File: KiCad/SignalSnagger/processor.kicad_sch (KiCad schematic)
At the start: 78 parts, among them J201 Conn_01x01_Female, J202 Conn_01x01_Female, J203 Conn_01x02, J204 Conn_01x02, J205 Conn_01x01_Female, J206 Conn_01x01_Female, J207 Conn_01x01_Female, J208 Conn_01x01_Female, J209 Conn_01x01_Female, J210 Conn_01x01_Female, J211 Conn_01x01_Female, J212 Conn_01x01_Female, J213 Conn_01x01_Female, J214 Conn_01x01_Female, J215 Conn_01x01_Female, J216 Conn_01x01_Female, J217 Conn_01x01_Female, P201 ISP/PDI, Q201 BSS84W-7-F, Q202 BSS138W-7-F, SW201 SW_SPST, SW202 SW_SPST, SW203 PEC12R-4225F-S0024, U201 AVR128DA48, U202 SI5351, U203 LP2985-5.0, U204 LP2985-3.3, U205 EA_DOGS104W-A, U206 LP2985-5.0, U207 MAX1683EUK, X201 ECS-327TXO-30-TR, X202 25 MHz

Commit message: Ver 0.309
PCB layout updates
Schematic updates
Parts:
- added J218, J219, J220, J221: Conn_01x02, Connector_PinSocket_1.27mm:PinSocket_1x02_P1.27mm_Vertical, symbol Connector_Generic:Conn_01x02
- added SW204, SW205: SW_SPST, Button_Switch_SMD:SW_SPST_TL1014BF160QG, symbol Switch:SW_SPST
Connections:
- net GND: now also J218.1 (Pin_1), J219.1 (Pin_1)
- net PA0: now also J218.2 (Pin_2)
- net PA1: now also J219.2 (Pin_2)
- new net: J221.1 (Pin_1), SW205.1 (A)
- new net: J221.2 (Pin_2), SW205.2 (B)
- new net: J220.1 (Pin_1), SW204.1 (A)
- new net: J220.2 (Pin_2), SW204.2 (B)
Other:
- note removed: "Sense 2"
- moved on the sheet: SW201, SW202

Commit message: Ver 0.310
Schematic and PCB updates
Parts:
- added JP202: Jumper_2_Bridged, Jumper:Jumper_THT-1x02_Bridged_Circular, symbol Jumper:Jumper_2_Bridged_THT
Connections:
- net GND: now also JP202.2 (B); no longer C202.1, C203.1, C205.1, C206.1, C208.2, C209.1, C211.1, C212.1, C213.2, C214.2, C215.2, C216.1, C217.2, C218.1, C219.2, C221.1, D203.1 (K), D204.1 (K), J203.1 (Pin_1), J204.1 (Pin_1), J218.1 (Pin_1), J219.1 (Pin_1), P201.6 (Pin_6), SW201.2 (B), SW202.2 (B), SW203.C, SW203.S2, TP201.1 (Pin_1), U201.15 (GND), U201.29 (GND), U201.43 (GND), U202.8 (GND), U204.2 (GND), U205.12 (IM1), U205.14 (VSS), U205.18 (~{CS}), U205.19 (SA0), X201.2 (GND), X202.2 (GND)
- new net GNDD: C202.1, C203.1, C205.1, C206.1, C208.2, C209.1, C211.1, C212.1, C213.2, C214.2, C215.2, C216.1, C217.2, C218.1, C219.2, C221.1, D203.1 (K), D204.1 (K), J203.1 (Pin_1), J204.1 (Pin_1), J218.1 (Pin_1), J219.1 (Pin_1), JP202.1 (A), P201.6 (Pin_6), SW201.2 (B), SW202.2 (B), SW203.C, SW203.S2, TP201.1 (Pin_1), U201.15 (GND), U201.29 (GND), U201.43 (GND), U202.8 (GND), U204.2 (GND), U205.12 (IM1), U205.14 (VSS), U205.18 (~{CS}), U205.19 (SA0), X201.2 (GND), X202.2 (GND)
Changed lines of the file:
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@@
     (title "SignalSnagger")
     (date "2024-03-18")
-    (rev "0.309")
+    (rev "0.310")
   )
   (bus_alias "PROC_BUS" (members "PA7" "PA6" "PA5" "PA4" "PA3" "PA2" "PA1" "PA0" "PB5" "PB4" "SCL1" "SDA1" "PB1" "PB0" "PC7" "PC6" "PC5" "PC4" "SCL0" "SDA0" "RXD1" "TXD1" "ADC7" "DAC0" "ADC5" "ADC4" "ADC3" "ADC2" "ADC1" "ADC0" "PE3" "PE2" "RXD4" "TXD4" "PF6" "PF5" "PF4" "PF3" "PF2"))
@@
     (stroke (width 0) (type default) (color 0 0 0 0))
   )
+  (wire (pts (xy 36.83 190.5) (xy 36.83 187.96))
+    (stroke (width 0) (type default) (color 0 0 0 0))
+  )
   (wire (pts (xy 240.03 127) (xy 240.03 121.92))
     (stroke (width 0) (type default) (color 0 0 0 0))
@@
     (stroke (width 0) (type default) (color 0 0 0 0))
   )
-  (wire (pts (xy 40.64 190.5) (xy 40.64 189.23))
-    (stroke (width 0) (type default) (color 0 0 0 0))
-  )
   (wire (pts (xy 91.44 55.88) (xy 93.98 55.88))
     (stroke (width 0) (type default) (color 0 0 0 0))
@@
     (stroke (width 0) (type default) (color 0 0 0 0))
   )
-  (wire (pts (xy 45.72 189.23) (xy 45.72 191.77))
-    (stroke (width 0) (type default) (color 0 0 0 0))
-  )
   (wire (pts (xy 266.7 121.92) (xy 274.32 121.92))
     (stroke (width 0) (type default) (color 0 0 0 0))
@@
     (stroke (width 0) (type default) (color 0 0 0 0))
   )
-  (wire (pts (xy 40.64 189.23) (xy 45.72 189.23))
-    (stroke (width 0) (type default) (color 0 0 0 0))
-  )
   (wire (pts (xy 280.67 107.95) (xy 274.32 107.95))
     (stroke (width 0) (type default) (color 0 0 0 0))
@@
     (stroke (width 0) (type default) (color 0 0 0 0))
   )
+  (wire (pts (xy 26.67 190.5) (xy 26.67 187.96))
+    (stroke (width 0) (type default) (color 0 0 0 0))
+  )
   (wire (pts (xy 127 144.78) (xy 132.08 144.78))
     (stroke (width 0) (type default) (color 0 0 0 0))
@@
     (pin "1")
   )
+  (symbol (lib_id "Jumper:Jumper_2_Bridged_THT") (at 31.75 187.96 0) (unit 1)
+    (in_bom yes) (on_board yes)
+    (property "Reference" "JP202" (id 0) (at 31.75 189.23 90)
+      (effects (font (size 1.27 1.27)) (justify right))
+    )
+    (property "Value" "Jumper_2_Bridged" (id 1) (at 31.75 186.1621 0)
+      (effects (font (size 1.27 1.27)) hide)
+    )
+    (property "Footprint" "Jumper:Jumper_THT-1x02_Bridged_Circular" (id 2) (at 31.75 187.96 0)
+      (effects (font (size 1.27 1.27)) hide)
+    )
+    (property "Datasheet" "~" (id 3) (at 31.75 187.96 0)
+      (effects (font (size 1.27 1.27)) hide)
+    )
+    (property "Digi-Key Part No." "N/P" (id 4) (at 31.75 187.96 0)
+      (effects (font (size 1.27 1.27)) hide)
+    )
+    (pin "1")
+    (pin "2")
+  )
   (symbol (lib_id "power:GNDD") (at 147.32 149.86 90) (mirror x) (unit 1)
     (in_bom yes) (on_board yes)
@@
     (pin "1")
   )
-  (symbol (lib_id "power:GNDD") (at 40.64 190.5 0) (unit 1)
+  (symbol (lib_id "power:GNDD") (at 26.67 190.5 0) (unit 1)
     (in_bom yes) (on_board yes) (fields_autoplaced)
-    (property "Reference" "#PWR0259" (id 0) (at 40.64 196.85 0)
+    (property "Reference" "#PWR0259" (id 0) (at 26.67 196.85 0)
       (effects (font (size 1.27 1.27)) hide)
     )
-    (property "Value" "GNDD" (id 1) (at 40.64 194.5624 0))
-    (property "Footprint" "" (id 2) (at 40.64 190.5 0)
+    (property "Value" "GNDD" (id 1) (at 26.67 194.5624 0))
+    (property "Footprint" "" (id 2) (at 26.67 190.5 0)
       (effects (font (size 1.27 1.27)) hide)
     )
-    (property "Datasheet" "" (id 3) (at 40.64 190.5 0)
+    (property "Datasheet" "" (id 3) (at 26.67 190.5 0)
       (effects (font (size 1.27 1.27)) hide)
     )
@@
     (pin "2")
   )
-  (symbol (lib_id "power:GND") (at 45.72 191.77 0) (unit 1)
+  (symbol (lib_id "power:GND") (at 36.83 190.5 0) (unit 1)
     (in_bom yes) (on_board yes) (fields_autoplaced)
-    (property "Reference" "#PWR0260" (id 0) (at 45.72 198.12 0)
-      (effects (font (size 1.27 1.27)) hide)
-    )
-    (property "Value" "GND" (id 1) (at 45.72 196.2134 0)
+    (property "Reference" "#PWR0260" (id 0) (at 36.83 196.85 0)
       (effects (font (size 1.27 1.27)) hide)
     )
-    (property "Footprint" "" (id 2) (at 45.72 191.77 0)
+    (property "Value" "GND" (id 1) (at 36.83 194.9434 0))
+    (property "Footprint" "" (id 2) (at 36.83 190.5 0)
       (effects (font (size 1.27 1.27)) hide)
     )
-    (property "Datasheet" "" (id 3) (at 45.72 191.77 0)
+    (property "Datasheet" "" (id 3) (at 36.83 190.5 0)
       (effects (font (size 1.27 1.27)) hide)
     )

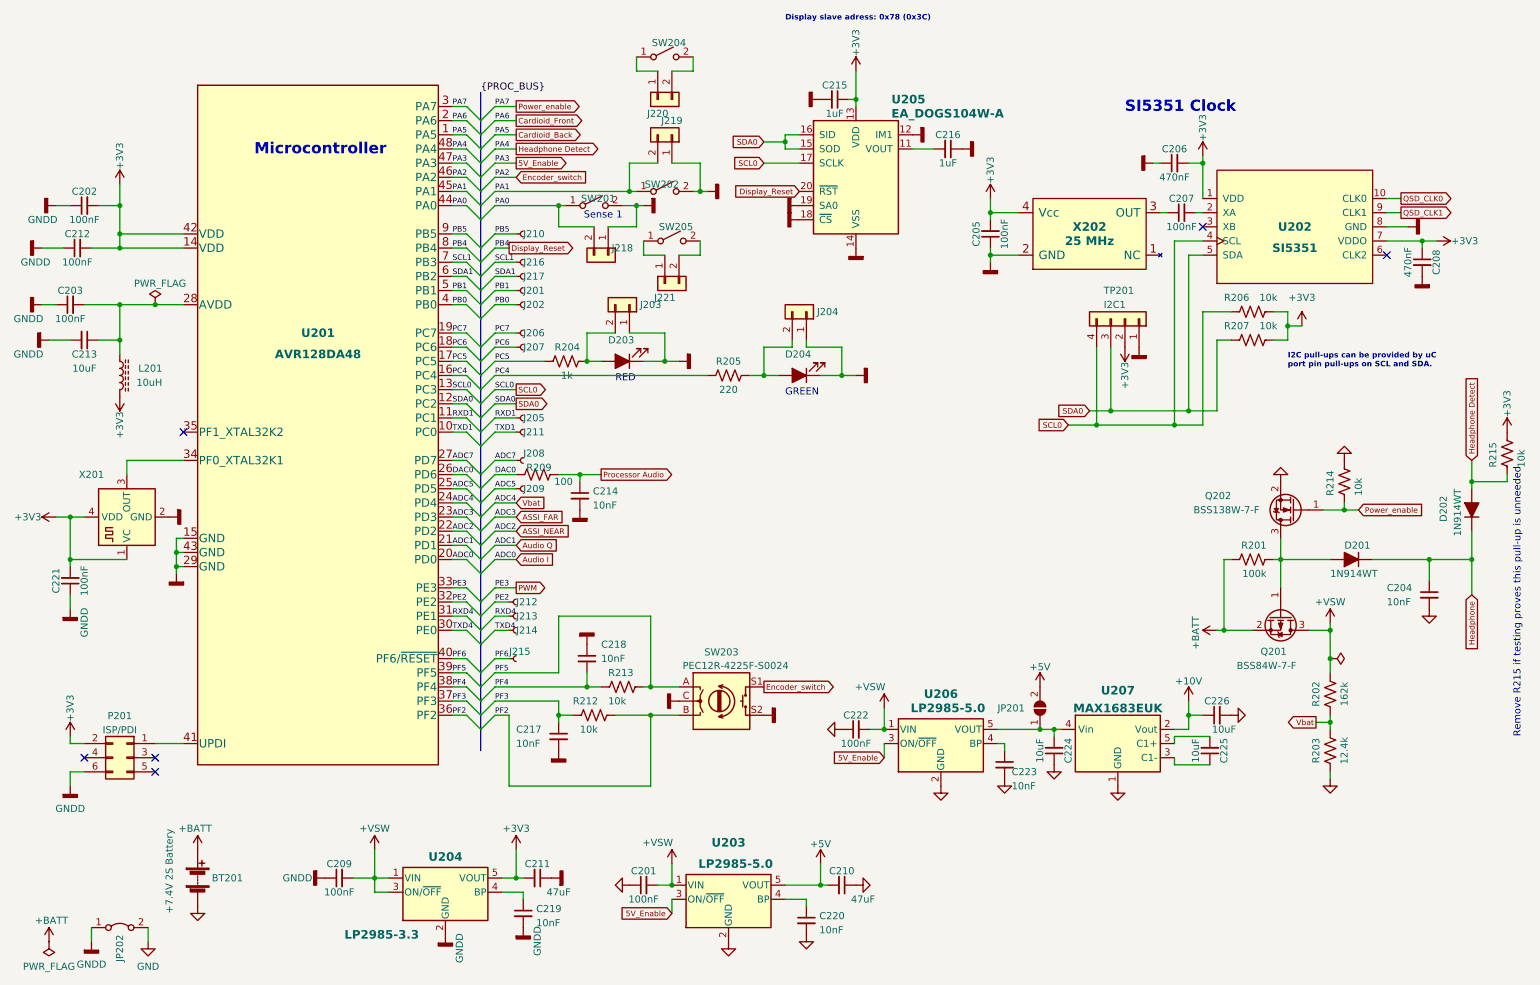
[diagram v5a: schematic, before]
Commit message: Ver 0.311
Schematic and PCB updates
All PCB connections have been made
Design rule check returns no errors or warnings
Still need to examine footprints, trace widths, pour coverage, etc.
First Gerbers built
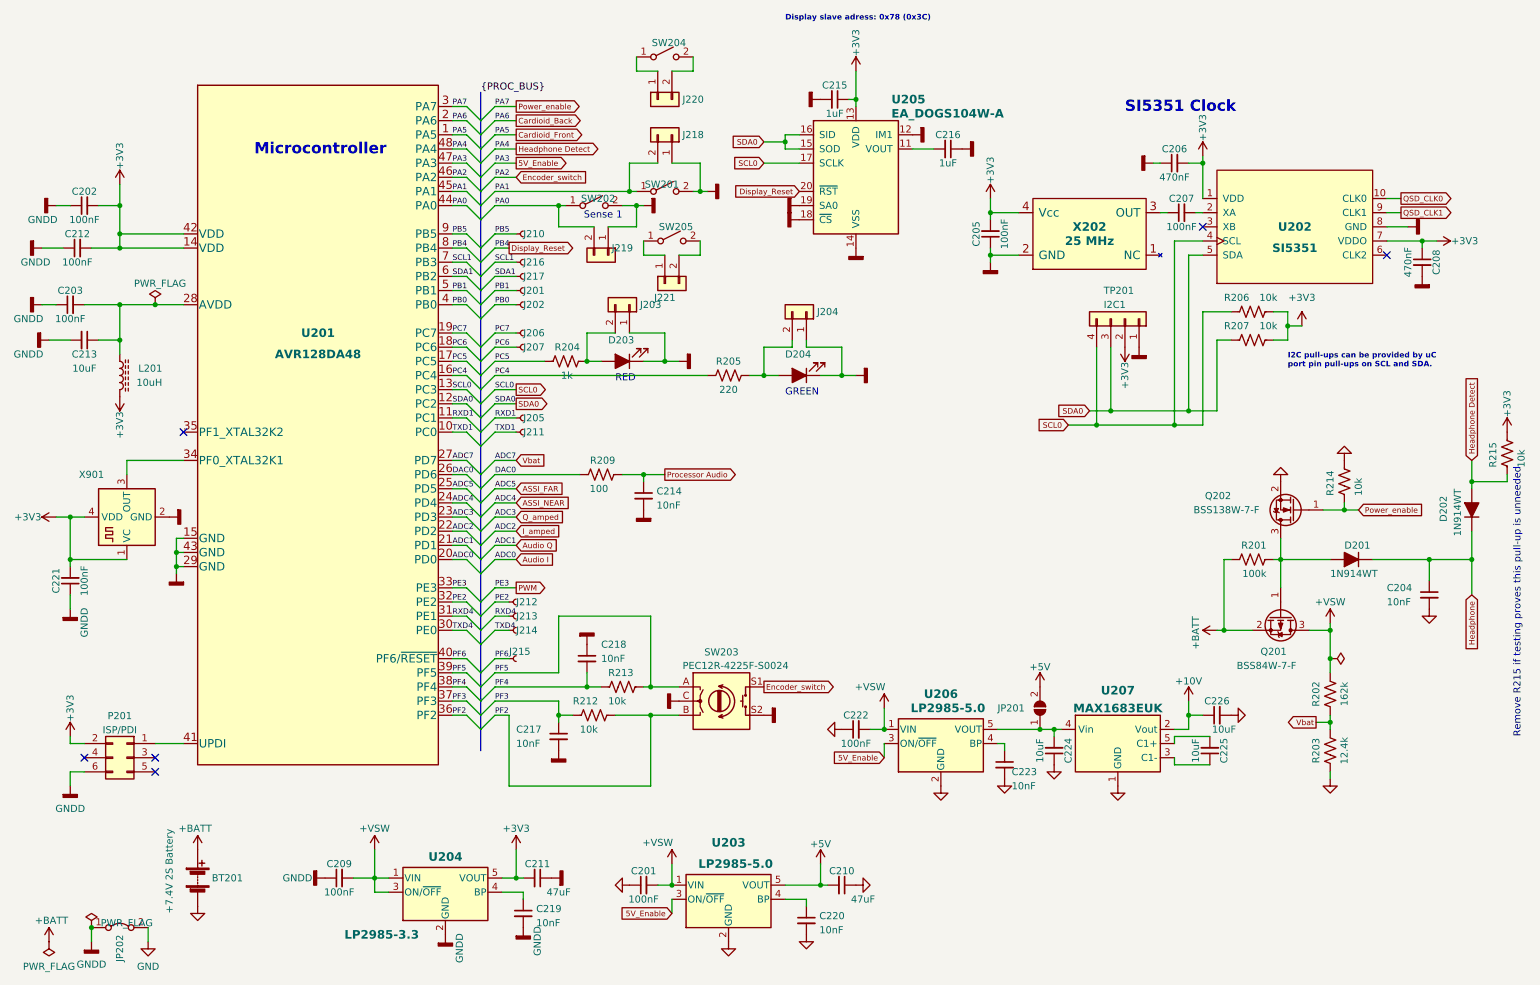
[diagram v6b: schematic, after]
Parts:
- removed J208, J209: Conn_01x01_Female, Oddities:Dummy_Empty, symbol Connector:Conn_01x01_Generic
- renumbered J219 to J218, J218 to J219, SW202 to SW201, SW201 to SW202, X201 to X901
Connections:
- net ADC5 is gone; now on net ASSI_FAR: U201.25 (PD5)
- net ADC7 is gone; now on net Vbat: U201.27 (PD7)
- net ASSI_FAR: no longer U201.23 (PD3)
- net ASSI_NEAR: now also U201.24 (PD4); no longer U201.22 (PD2)
- net Cardioid_Back: now also U201.2 (PA6); no longer U201.1 (PA5)
- net Cardioid_Front: now also U201.1 (PA5); no longer U201.2 (PA6)
- net Vbat: no longer U201.24 (PD4)
- new net I_amped: U201.22 (PD2)
- new net Q_amped: U201.23 (PD3)
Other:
- moved on the sheet: C214, R209

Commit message: Ver 0.312
PCB updates
BOM updates
Schematic updates
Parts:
- P201: Digi-Key Part No. 137-35RASMT2BHSNTRXCT-ND -> M20-8760442-ND; Link https://www.digikey.com/en/products/detail/switchcraft-inc/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 -> https://www.digikey.com/en/products/detail/harwin-inc/M20-8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; Manufacturer Switchcraft Inc. -> Harwin Inc.; Manufacturer PN 35RASMT2BHSNTRX -> M20-8760442
- SW204, SW205: Digi-Key Part No. EG5042CT-ND -> N/P
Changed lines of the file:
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@@
   (title_block
     (title "SignalSnagger")
-    (date "2024-03-27")
-    (rev "0.311")
+    (date "2024-03-29")
+    (rev "0.312")
   )
   (bus_alias "PROC_BUS" (members "PA7" "PA6" "PA5" "PA4" "PA3" "PA2" "PA1" "PA0" "PB5" "PB4" "SCL1" "SDA1" "PB1" "PB0" "PC7" "PC6" "PC5" "PC4" "SCL0" "SDA0" "RXD1" "TXD1" "ADC7" "DAC0" "ADC5" "ADC4" "ADC3" "ADC2" "ADC1" "ADC0" "PE3" "PE2" "RXD4" "TXD4" "PF6" "PF5" "PF4" "PF3" "PF2"))
@@
       (effects (font (size 1.27 1.27)) hide)
     )
-    (property "Digi-Key Part No." "EG5042CT-ND" (id 4) (at 130.81 64.77 0)
+    (property "Digi-Key Part No." "N/P" (id 4) (at 130.81 64.77 0)
       (effects (font (size 1.27 1.27)) hide)
     )
@@
       (effects (font (size 1.27 1.27)) hide)
     )
-    (property "Digi-Key Part No." "137-35RASMT2BHSNTRXCT-ND" (id 4) (at 33.02 157.48 0)
-      (effects (font (size 1.27 1.27)) hide)
-    )
-    (property "Link" "https://www.digikey.com/en/products/detail/switchcraft-inc/35rasmt2bhsntrx/16041219" (id 5) (at 33.02 157.48 0)
-      (effects (font (size 1.27 1.27)) hide)
-    )
-    (property "Manufacturer" "Switchcraft Inc." (id 6) (at 33.02 157.48 0)
-      (effects (font (size 1.27 1.27)) hide)
-    )
-    (property "Manufacturer PN" "35RASMT2BHSNTRX" (id 7) (at 33.02 157.48 0)
-      (effects (font (size 1.27 1.27)) hide)
-    )
-    (property "Description" "3.5MM SURFACE MOUNT JACK, STEREO" (id 8) (at 33.02 157.48 0)
+    (property "Digi-Key Part No." "M20-8760442-ND" (id 4) (at 33.02 157.48 0)
+      (effects (font (size 1.27 1.27)) hide)
+    )
+    (property "Link" "https://www.digikey.com/en/products/detail/harwin-inc/M20-8760442/3919929" (id 5) (at 33.02 157.48 0)
+      (effects (font (size 1.27 1.27)) hide)
+    )
+    (property "Manufacturer" "Harwin Inc." (id 6) (at 33.02 157.48 0)
+      (effects (font (size 1.27 1.27)) hide)
+    )
+    (property "Manufacturer PN" "M20-8760442" (id 7) (at 33.02 157.48 0)
+      (effects (font (size 1.27 1.27)) hide)
+    )
+    (property "Description" "CONN HEADER SMD 8POS 2.54MM" (id 8) (at 33.02 157.48 0)
       (effects (font (size 1.27 1.27)) hide)
     )
@@
       (effects (font (size 1.27 1.27)) hide)
     )
-    (property "Digi-Key Part No." "EG5042CT-ND" (id 4) (at 129.54 31.75 0)
-      (effects (font (size 1.27 1.27)) hide)
-    )
+    (property "Digi-Key Part No." "N/P" (id 4) (at 129.54 31.75 0)
+      (effects (font (size 1.27 1.27)) hide)
+    )
